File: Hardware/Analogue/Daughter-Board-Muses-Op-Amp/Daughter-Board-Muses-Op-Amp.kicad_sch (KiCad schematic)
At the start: 39 parts, among them J1 Audio In, J12 Digital Power, J13 Audio In Left, J14 Audio In Right, J15 Buffer Power, J18 Buffer Out Right, J19 Buffer Out Left, J2 Audio Out, J3 Conn_01x03_Female, J4 Digital In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

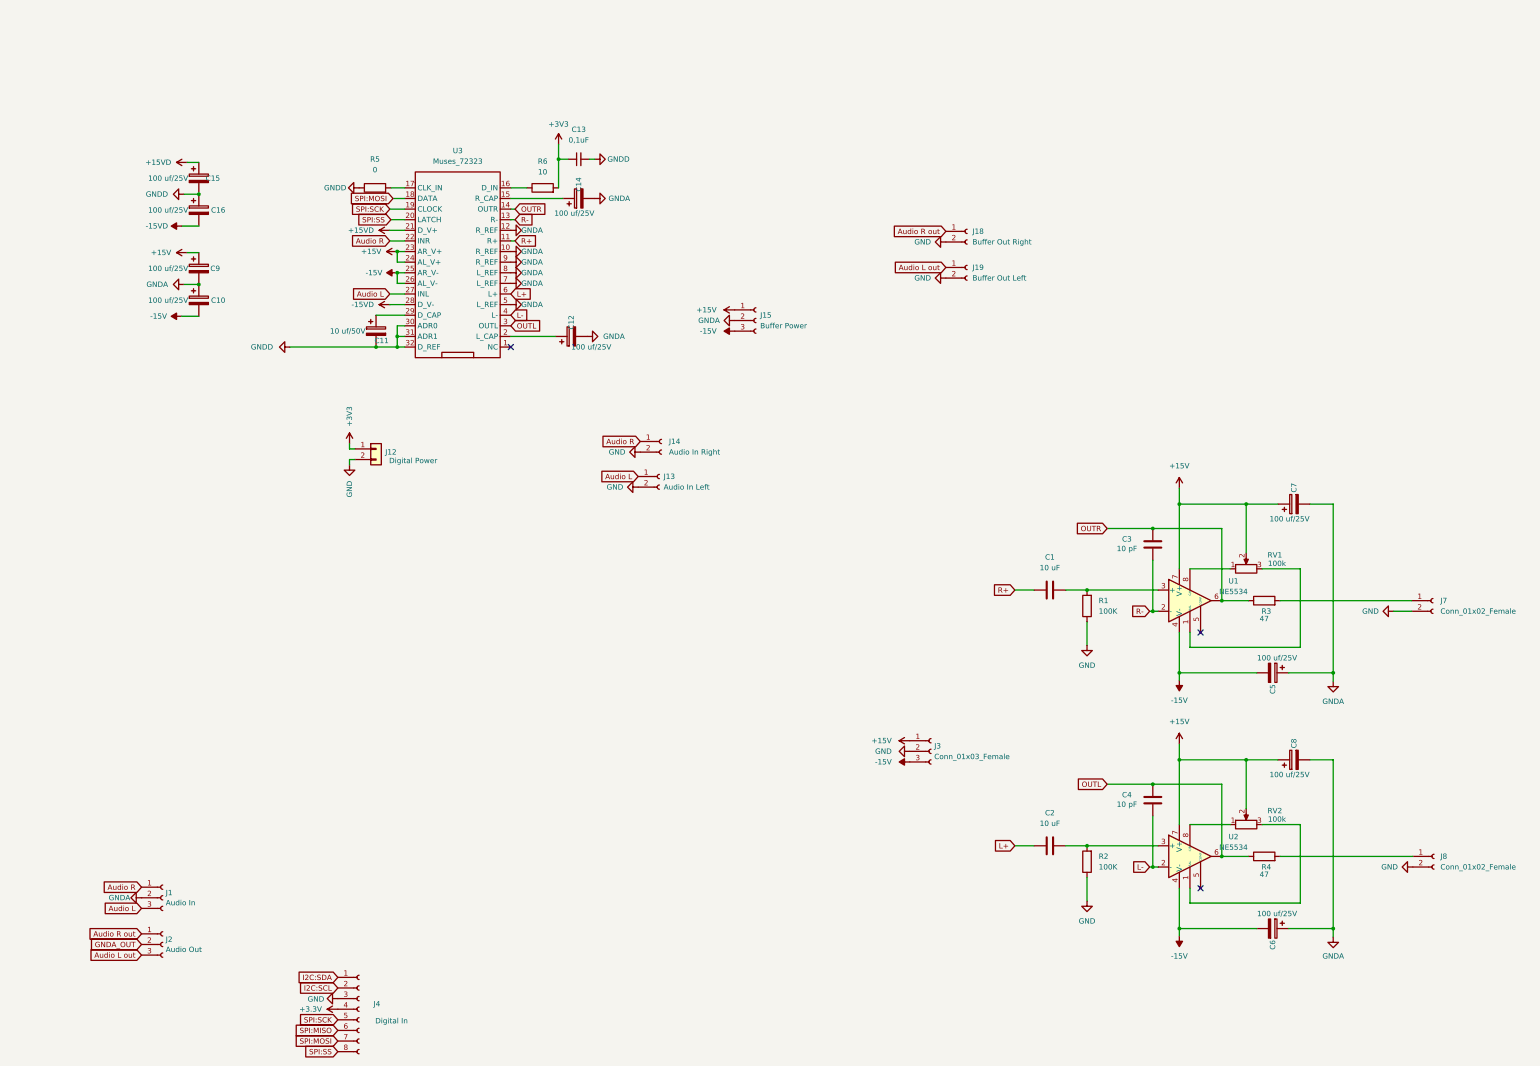
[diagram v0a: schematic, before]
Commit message: daughter board muses + buffer
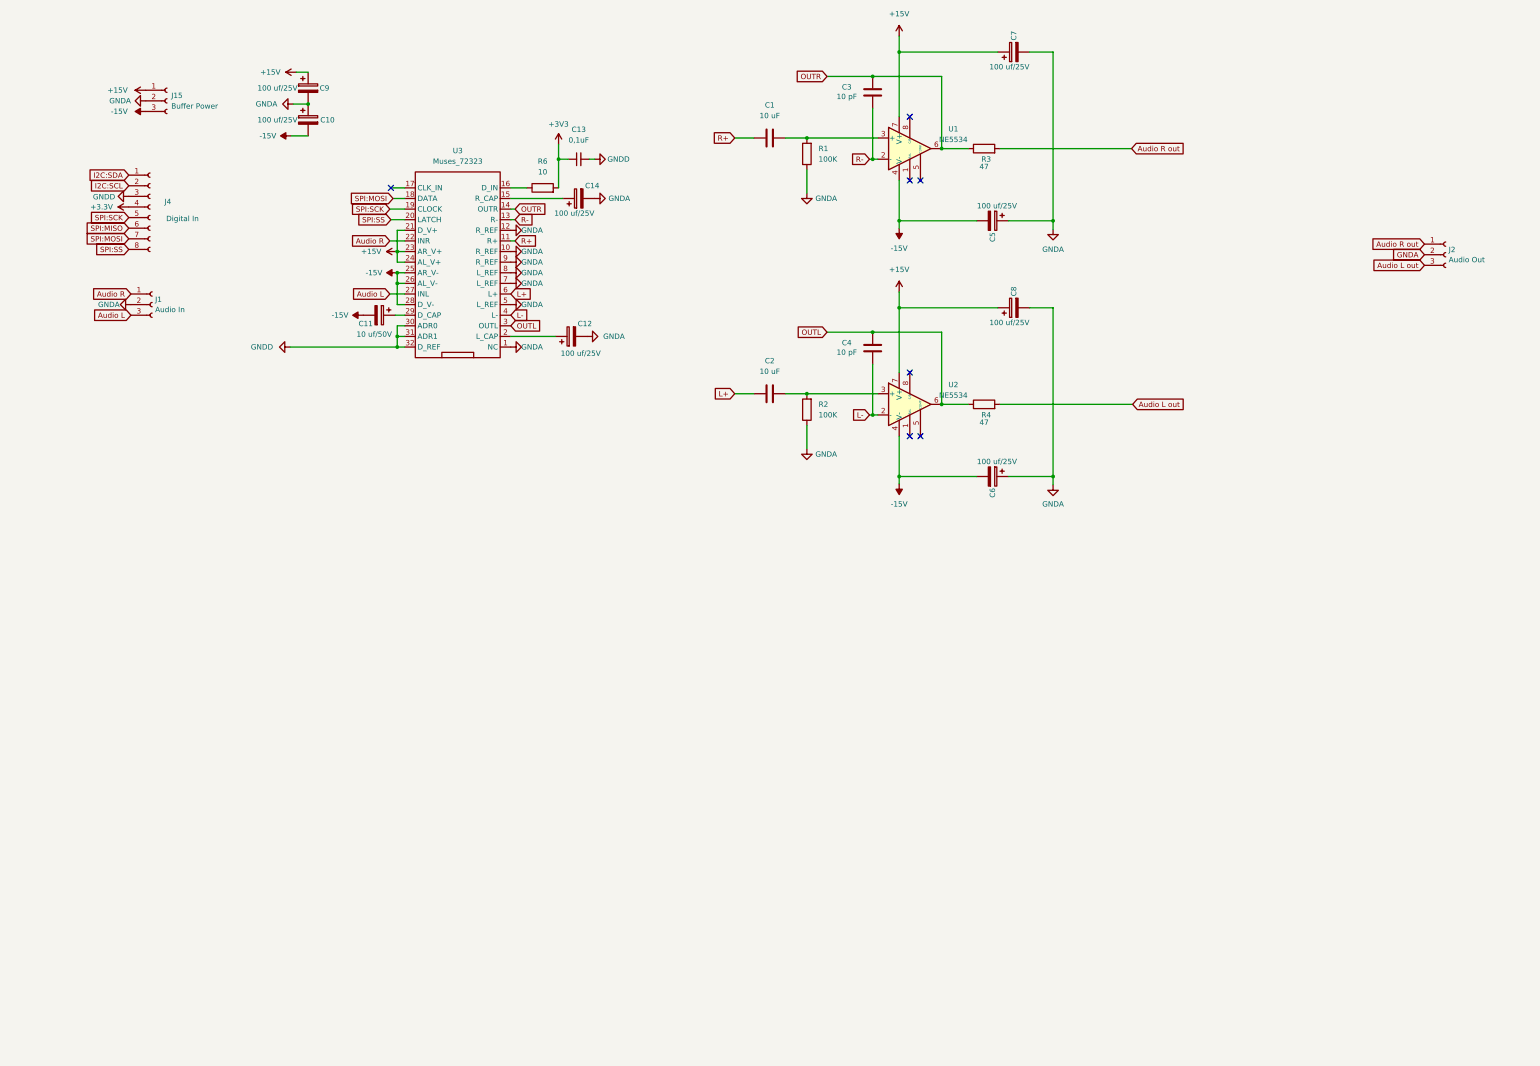
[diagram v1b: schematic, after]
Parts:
- removed C15, C16: 100 uf/25V, Capacitor_THT:CP_Radial_D8.0mm_P3.50mm, symbol Device:C_Polarized
- removed J12: Digital Power, TerminalBlock:TerminalBlock_bornier-2_P5.08mm, symbol Connector_Generic:Conn_01x02
- removed J13: Audio In Left, Connector_PinHeader_2.54mm:PinHeader_1x02_P2.54mm_Vertical, symbol Connector:Conn_01x02_Female
- removed J14: Audio In Right, Connector_PinHeader_2.54mm:PinHeader_1x02_P2.54mm_Vertical, symbol Connector:Conn_01x02_Female
- removed J18: Buffer Out Right, Connector_PinHeader_2.54mm:PinHeader_1x02_P2.54mm_Vertical, symbol Connector:Conn_01x02_Female
- removed J19: Buffer Out Left, Connector_PinHeader_2.54mm:PinHeader_1x02_P2.54mm_Vertical, symbol Connector:Conn_01x02_Female
- removed J3: Conn_01x03_Female, Connector_PinHeader_2.54mm:PinHeader_1x03_P2.54mm_Vertical, symbol Connector:Conn_01x03_Female
- removed J7, J8: Conn_01x02_Female, Connector_PinHeader_2.54mm:PinHeader_1x02_P2.54mm_Vertical, symbol Connector:Conn_01x02_Female
- removed R5: 0, symbol Device:R
- removed RV1, RV2: 100k, Potentiometer_THT:Potentiometer_Bourns_3296W_Vertical, symbol Device:R_Potentiometer
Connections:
- net +15VD is gone; now on net +15V: U3.21 (D_V+)
- net -15VD is gone; now on net -15V: U3.28 (D_V-)
- net GNDA_OUT is gone; now on net GNDA: J2.2 (Pin_2)
- net -15V: now also C11.2
- net Audio L out: now also R4.2
- net Audio R out: now also R3.2
- net GNDA: now also R1.1, R2.1, U3.1 (NC)
- net GNDD: now also J4.3 (Pin_3); no longer C11.2
- removed net GND: J4.3 (Pin_3), R1.1, R2.1
- no-connect marks 3 -> 7
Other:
- moved on the sheet: C1, C10, C11, C2, C3, C4, C5, C6, C7, C8, C9, J1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

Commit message: PCB Daughter board started
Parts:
- added Q1, Q2, Q3, Q4: 2SK30, Package_TO_SOT_THT:TO-92, symbol PCM_Transistor_JFET_AKL:2SK30
- added R10, R11, R5, R7: 220, Resistor_SMD:R_0805_2012Metric_Pad1.20x1.40mm_HandSolder, symbol Device:R
- added R12, R13: 1M, Resistor_SMD:R_0805_2012Metric_Pad1.20x1.40mm_HandSolder, symbol Device:R
- added R8, R9: 220K, Resistor_SMD:R_0805_2012Metric_Pad1.20x1.40mm_HandSolder, symbol Device:R
- C13: footprint Capacitor_SMD:C_0805_2012Metric_Pad1.15x1.40mm_HandSolder -> Capacitor_SMD:C_0805_2012Metric_Pad1.18x1.45mm_HandSolder
- R1, R2, R3, R4: footprint Resistor_THT:R_Axial_DIN0207_L6.3mm_D2.5mm_P10.16mm_Horizontal -> Resistor_SMD:R_0805_2012Metric_Pad1.20x1.40mm_HandSolder
- R6: footprint (none) -> Resistor_SMD:R_0805_2012Metric_Pad1.20x1.40mm_HandSolder
- U3: footprint Muses72323v:SOP65P760X145-32N -> PCM_Package_SO_AKL:SSOP-32_11.305x20.495mm_P1.27mm
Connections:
- net +15V: now also Q1.3 (D), Q3.3 (D)
- net -15V: now also Q2.1 (S), Q2.2 (G), Q4.1 (S), Q4.2 (G)
- net Audio L: now also R10.2, R9.1; no longer U3.27 (INL)
- net Audio R: now also R7.2, R8.1; no longer U3.22 (INR)
- net GNDA: now also R12.2, R13.2, R8.2, R9.2
- net OUTL: no longer C4.1
- new net: Q3.1 (S), Q4.3 (D), R11.2
- new net: Q3.2 (G), R10.1
- new net: Q1.1 (S), Q2.3 (D), R5.2
- new net: Q1.2 (G), R7.1
- new net Buffer L: R11.1, R13.1, U3.27 (INL)
- new net Buffer R: R12.1, R5.1, U3.22 (INR)

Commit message: started pcb tracks
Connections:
- net +3.3V is gone; now on net +3V3: J4.4 (Pin_4)
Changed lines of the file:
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@@
 			)
 		)
-		(property "Value" "+3.3V"
-			(at 59.182 60.7059 90)
+		(property "Value" "+3V3"
+			(at 64.77 60.7059 90)
 			(effects
 				(font
 					(size 1.27 1.27)
 				)
-				(justify left)
+				(justify right)
 			)
 		)

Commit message: almost there with pcb again
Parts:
- C1, C2: footprint Capacitor_THT:CP_Radial_D6.3mm_P2.50mm -> Capacitor_THT:CP_Radial_D5.0mm_P2.00mm
- C11: footprint Capacitor_THT:CP_Radial_D8.0mm_P3.50mm -> Capacitor_THT:CP_Radial_D5.0mm_P2.00mm
- C3, C4: footprint Capacitor_THT:C_Disc_D4.3mm_W1.9mm_P5.00mm -> Capacitor_SMD:C_0805_2012Metric_Pad1.18x1.45mm_HandSolder
- Q1, Q2, Q3, Q4: value 2SK30 -> 2SK170; footprint Package_TO_SOT_THT:TO-92 -> PCM_Package_TO_SOT_THT_AKL:TO-92L_Inline; symbol PCM_Transistor_JFET_AKL:2SK30 -> Toshiba 2sk170:2SK170
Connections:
- net +15V: now also Q1.1 (D), Q3.1 (D); no longer Q1.3 (D), Q3.3 (D)
- net -15V: now also Q2.3 (S), Q4.3 (S); no longer Q2.1 (S), Q4.1 (S)
- net OUTL: now also C4.1
- new net: Q3.3 (S), Q4.1 (D), R11.2
- new net: Q1.3 (S), Q2.1 (D), R5.2
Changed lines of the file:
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@@
 	)
 	(junction
+		(at 241.046 90.678)
+		(diameter 0)
+		(color 0 0 0 0)
+	)
+	(junction
 		(at 76.708 163.068)
 		(diameter 0)
@@
 	(wire
 		(pts
-			(xy 230.124 90.678) (xy 257.556 90.678)
+			(xy 230.124 90.678) (xy 241.046 90.678)
 		)
 		(stroke
@@
 	(wire
 		(pts
+			(xy 241.046 90.678) (xy 257.556 90.678)
+		)
+		(stroke
+			(width 0)
+			(type default)
+		)
+	)
+	(wire
+		(pts
 			(xy 98.298 205.74) (xy 103.378 205.74)
 		)
@@
 	(wire
 		(pts
+			(xy 241.046 90.678) (xy 241.046 90.932)
+		)
+		(stroke
+			(width 0)
+			(type default)
+		)
+	)
+	(wire
+		(pts
 			(xy 127.254 66.294) (xy 127.254 71.374)
 		)
@@
 	)
 	(symbol
-		(lib_id "PCM_Transistor_JFET_AKL:2SK30")
+		(lib_id "Toshiba 2sk170:2SK170")
 		(at 73.914 199.39 0)
 		(unit 1)
@@
 		(fields_autoplaced yes)
 		(property "Reference" "Q3"
-			(at 79.502 198.1199 0)
+			(at 78.74 198.1199 0)
 			(effects
 				(font
@@
 			)
 		)
-		(property "Value" "2SK30"
-			(at 79.502 200.6599 0)
+		(property "Value" "2SK170"
+			(at 78.74 200.6599 0)
 			(effects
 				(font
@@
 			)
 		)
-		(property "Footprint" "Package_TO_SOT_THT:TO-92"
+		(property "Footprint" "PCM_Package_TO_SOT_THT_AKL:TO-92L_Inline"
 			(at 78.994 196.85 0)
 			(effects
@@
 			)
 		)
-		(property "Description" "TO-92 N-JFET transistor, 50V, 0.3mA, 100mW, Alternate KiCAD Library"
+		(property "Description" "TO-92 N-JFET transistor, 40V, 10mA, 400mW, Alternate KiCAD Library"
 			(at 73.914 199.39 0)
 			(effects
@@
 			)
 		)
-		(property "Footprint" "Capacitor_THT:CP_Radial_D6.3mm_P2.50mm"
+		(property "Footprint" "Capacitor_THT:CP_Radial_D5.0mm_P2.00mm"
 			(at 220.218 104.4448 0)
 			(effects
@@
 			)
 		)
-		(property "Footprint" "Capacitor_THT:CP_Radial_D6.3mm_P2.50mm"
+		(property "Footprint" "Capacitor_THT:CP_Radial_D5.0mm_P2.00mm"
 			(at 220.218 43.2308 0)
 			(effects
@@
 	)
 	(symbol
-		(lib_id "PCM_Transistor_JFET_AKL:2SK30")
+		(lib_id "Toshiba 2sk170:2SK170")
 		(at 74.168 155.956 0)
 		(unit 1)
@@
 		(fields_autoplaced yes)
 		(property "Reference" "Q2"
-			(at 79.756 154.6859 0)
+			(at 78.74 154.6859 0)
 			(effects
 				(font
@@
 			)
 		)
-		(property "Value" "2SK30"
-			(at 79.756 157.2259 0)
+		(property "Value" "2SK170"
+			(at 78.74 157.2259 0)
 			(effects
 				(font
@@
 			)
 		)
-		(property "Footprint" "Package_TO_SOT_THT:TO-92"
+		(property "Footprint" "PCM_Package_TO_SOT_THT_AKL:TO-92L_Inline"
 			(at 79.248 153.416 0)
 			(effects
@@
 			)
 		)
-		(property "Description" "TO-92 N-JFET transistor, 50V, 0.3mA, 100mW, Alternate KiCAD Library"
+		(property "Description" "TO-92 N-JFET transistor, 40V, 10mA, 400mW, Alternate KiCAD Library"
 			(at 74.168 155.956 0)
 			(effects
@@
 			)
 		)
-		(property "Footprint" "Capacitor_THT:C_Disc_D4.3mm_W1.9mm_P5.00mm"
+		(property "Footprint" "Capacitor_SMD:C_0805_2012Metric_Pad1.18x1.45mm_HandSolder"
 			(at 242.0112 37.084 0)
 			(effects
@@
 	)
 	(symbol
-		(lib_id "PCM_Transistor_JFET_AKL:2SK30")
+		(lib_id "Toshiba 2sk170:2SK170")
 		(at 74.168 141.732 0)
 		(unit 1)
@@
 		(fields_autoplaced yes)
 		(property "Reference" "Q1"
-			(at 79.756 140.4619 0)
+			(at 78.74 140.4619 0)
 			(effects
 				(font
@@
 			)
 		)
-		(property "Value" "2SK30"
-			(at 79.756 143.0019 0)
+		(property "Value" "2SK170"
+			(at 78.74 143.0019 0)
 			(effects
 				(font
@@
 			)
 		)
-		(property "Footprint" "Package_TO_SOT_THT:TO-92"
+		(property "Footprint" "PCM_Package_TO_SOT_THT_AKL:TO-92L_Inline"
 			(at 79.248 139.192 0)
 			(effects
@@
 			)
 		)
-		(property "Description" "TO-92 N-JFET transistor, 50V, 0.3mA, 100mW, Alternate KiCAD Library"
+		(property "Description" "TO-92 N-JFET transistor, 40V, 10mA, 400mW, Alternate KiCAD Library"
 			(at 74.168 141.732 0)
 			(effects
@@
 	)
 	(symbol
-		(lib_id "PCM_Transistor_JFET_AKL:2SK30")
+		(lib_id "Toshiba 2sk170:2SK170")
 		(at 73.914 213.614 0)
 		(unit 1)
@@
 		(fields_autoplaced yes)
 		(property "Reference" "Q4"
-			(at 79.502 212.3439 0)
+			(at 78.74 212.3439 0)
 			(effects
 				(font
@@
 			)
 		)
-		(property "Value" "2SK30"
-			(at 79.502 214.8839 0)
+		(property "Value" "2SK170"
+			(at 78.74 214.8839 0)
 			(effects
 				(font
@@
 			)
 		)
-		(property "Footprint" "Package_TO_SOT_THT:TO-92"
+		(property "Footprint" "PCM_Package_TO_SOT_THT_AKL:TO-92L_Inline"
 			(at 78.994 211.074 0)
 			(effects
@@
 			)
 		)
-		(property "Description" "TO-92 N-JFET transistor, 50V, 0.3mA, 100mW, Alternate KiCAD Library"
+		(property "Description" "TO-92 N-JFET transistor, 40V, 10mA, 400mW, Alternate KiCAD Library"
 			(at 73.914 213.614 0)
 			(effects
@@
 			)
 		)
-		(property "Footprint" "Capacitor_THT:C_Disc_D4.3mm_W1.9mm_P5.00mm"
+		(property "Footprint" "Capacitor_SMD:C_0805_2012Metric_Pad1.18x1.45mm_HandSolder"
 			(at 242.0112 98.552 0)
 			(effects
@@
 			)
 		)
-		(property "Footprint" "Capacitor_THT:CP_Radial_D8.0mm_P3.50mm"
+		(property "Footprint" "Capacitor_THT:CP_Radial_D5.0mm_P2.00mm"
 			(at 119.126 87.5792 0)
 			(effects

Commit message: pcb update
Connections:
- net Audio L: now also R7.2, R8.1; no longer R10.2, R9.1
- net Audio R: now also R10.2, R9.1; no longer R7.2, R8.1
- net Buffer L: now also R12.1, R5.1; no longer R11.1, R13.1
- net Buffer R: now also R11.1, R13.1; no longer R12.1, R5.1

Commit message: Footprints updated - rerouting still missing
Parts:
- Q1, Q2, Q3, Q4: footprint PCM_Package_TO_SOT_THT_AKL:TO-92L_Inline -> Package_TO_SOT_THT:TO-92_HandSolder
- U3: footprint PCM_Package_SO_AKL:SSOP-32_11.305x20.495mm_P1.27mm -> Muses:TSSOP-32_6.1x11mm_P0.65mm
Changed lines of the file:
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@@
 			)
 		)
-		(property "Footprint" "PCM_Package_TO_SOT_THT_AKL:TO-92L_Inline"
+		(property "Footprint" "Package_TO_SOT_THT:TO-92_HandSolder"
 			(at 78.994 196.85 0)
 			(effects
@@
 			)
 		)
-		(property "Footprint" "PCM_Package_SO_AKL:SSOP-32_11.305x20.495mm_P1.27mm"
+		(property "Footprint" "Muses:TSSOP-32_6.1x11mm_P0.65mm"
 			(at 154.432 94.234 0)
 			(effects
@@
 			)
 		)
-		(property "Footprint" "PCM_Package_TO_SOT_THT_AKL:TO-92L_Inline"
+		(property "Footprint" "Package_TO_SOT_THT:TO-92_HandSolder"
 			(at 79.248 153.416 0)
 			(effects
@@
 			)
 		)
-		(property "Footprint" "PCM_Package_TO_SOT_THT_AKL:TO-92L_Inline"
+		(property "Footprint" "Package_TO_SOT_THT:TO-92_HandSolder"
 			(at 79.248 139.192 0)
 			(effects
@@
 			)
 		)
-		(property "Footprint" "PCM_Package_TO_SOT_THT_AKL:TO-92L_Inline"
+		(property "Footprint" "Package_TO_SOT_THT:TO-92_HandSolder"
 			(at 78.994 211.074 0)
 			(effects
